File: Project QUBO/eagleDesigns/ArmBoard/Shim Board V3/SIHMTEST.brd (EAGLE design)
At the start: 71.1 x 81.3 mm, 30 parts, among them IC1 MCP2551/SN, U1 BME280

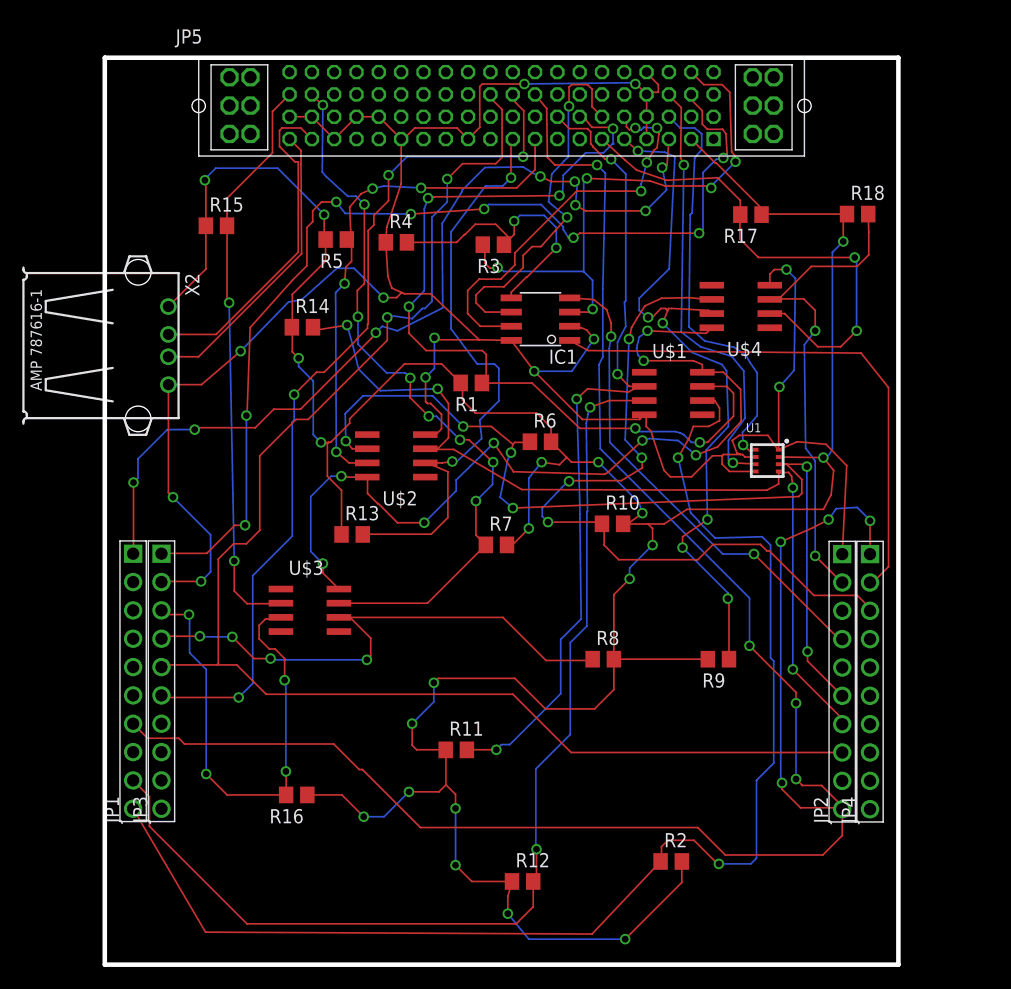
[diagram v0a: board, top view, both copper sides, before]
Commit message: 
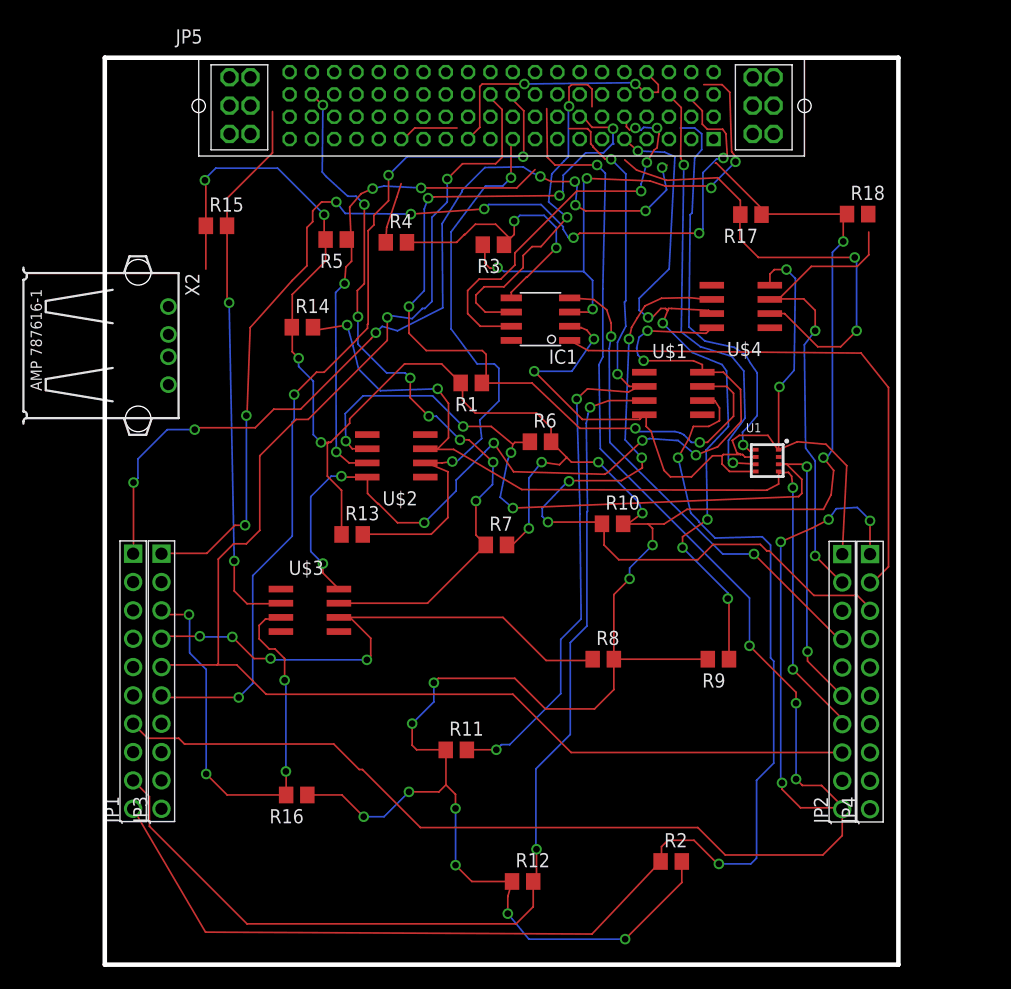
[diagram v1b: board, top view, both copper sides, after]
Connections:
- net N$11 renamed RX_CF
- net N$13 renamed CTS_CF
- net N$14 renamed RTS_CF
- net N$29 renamed CTS_MC
- net N$30 renamed RTS_MC
- net N$31 renamed PWM_0
- net N$48 renamed RX_SF
- net N$52 renamed CE_2
- net N$53 renamed CE_3
- net N$54 renamed CE_4
- net N$66 renamed RX_MD
- net N$67 renamed TX_MD
- net N$68 renamed CTS_MD
- net N$69 renamed RTS_MD
- net N$7 renamed RX_PF
- net N$73 renamed CE_LEDS
- net N$74 renamed CE_CPU
- net N$8 renamed TX_PF
- net UNBUFFERSCL0 renamed ACT_UNBUFFERSCL
- net UNBUFFERSCL1 renamed EXT_UNBUFFERSCL
- net UNBUFFERSCL2 renamed BATT_UNBUFFERSCL
- net UNBUFFERSCL3 renamed INT_UNBUFFERSCL
- net UNBUFFERSDA0 renamed ACT_UNBUFFERSDA
- net UNBUFFERSDA1 renamed EXT_UNBUFFERSDA
- net UNBUFFERSDA2 renamed BATT_UNBUFFERSDA
- net UNBUFFERSDA3 renamed INT_UNBUFFERSDA
- removed net 3.3(VDDBME): JP5.23, U1.P$8
- removed net 3.3(VDDIOBME): JP5.43, U1.P$6
- removed net 5.0(BME): JP5.2, R1.2, R10.2, R11.1, R12.1, R13.1, R14.1, R15.1, R16.1, R17.1, R18.1, R2.2, R5.2, R6.2, R7.2, R8.2, R9.2, U1.P$2, X2.1
- removed net BUFFERSCL0: JP5.28, R11.2, U$1.2
- removed net BUFFERSCL1: JP5.10, R13.2, U$2.2
- removed net BUFFERSCL2: JP5.60, R15.2, U$3.2
- removed net BUFFERSCL3: JP5.6, R17.2, U$4.2
- removed net BUFFERSDA0: JP5.27, R1.1, U$1.7
- removed net BUFFERSDA1: JP5.9, R5.1, U$2.7
- removed net BUFFERSDA2: JP5.59, R7.1, U$3.7
- removed net BUFFERSDA3: JP5.5, R9.1, U$4.7
- removed net BUFFERVCC(5V): JP5.22
- removed net GND: IC1.2, IC1.8, JP2.P$1, JP3.P$2, JP5.12, JP5.15, JP5.18, JP5.24, JP5.36, JP5.37, JP5.39, JP5.4, JP5.40, JP5.44, JP5.64, R4.1, U$1.4, U$2.4, U$4.4, U1.P$1, U1.P$5, U1.P$7, X2.4
- removed net GPIO_1: JP5.38
- removed net N$1: JP5.1
- removed net N$21: JP5.21
- removed net N$32: JP5.32
- removed net N$33: JP5.33
- removed net N$34: JP5.34
- removed net N$35: JP5.35
- removed net N$41: JP5.41
- removed net N$45: JP5.45
- removed net N$46: JP5.46
- removed net N$47: JP5.47
- removed net N$55: JP5.55
- removed net N$56: JP5.56
- removed net N$57: JP5.57
- removed net N$58: JP5.58
- removed net N$61: JP5.61
- removed net N$63: JP5.63
- removed net N$65: JP5.65
- removed net N$70: JP5.70
- removed net N$71: JP5.71
- removed net N$72: JP5.72
- removed net N$75: JP5.75
- removed net N$76: JP5.76
- removed net N$77: JP5.77
- removed net N$78: JP5.78
- removed net N$79: JP5.79
- removed net N$80: JP5.80
- removed net USB1+: JP5.17
- removed net USB1-: JP5.16
- removed net VDD: IC1.3, JP5.62, R3.2
- new net 12V: JP5.16, JP5.36, JP5.56, JP5.76
- new net 3.3V: JP5.18, JP5.38, JP5.58, JP5.78, U1.P$6, U1.P$8
- new net 5V: IC1.3, JP5.17, JP5.37, JP5.57, JP5.77, R1.2, R10.2, R11.1, R12.1, R13.1, R14.1, R15.1, R16.1, R17.1, R18.1, R2.2, R3.2, R5.2, R6.2, R7.2, R8.2, R9.2, U1.P$2, X2.1
- new net ACT_SCL: JP5.24, R11.2, U$1.2
- new net ACT_SDA: JP5.23, R1.1, U$1.7
- new net AGND: JP5.19, JP5.20, JP5.39, JP5.40, JP5.59, JP5.60, JP5.79, JP5.80
- new net BATT_SCL: JP5.44, R15.2, U$3.2
- new net BATT_SDA: JP5.43, R7.1, U$3.7
- new net CTS_MF: JP5.5
- new net CTS_PF: JP5.9
- new net CTS_SF: JP5.50
- new net DGND: IC1.2, IC1.8, JP2.P$1, JP3.P$2, JP5.1, JP5.15, JP5.21, JP5.25, JP5.32, JP5.35, JP5.47, JP5.55, JP5.63, JP5.75, R4.1, U$1.4, U$2.4, U$4.4, U1.P$1, U1.P$5, U1.P$7, X2.4
- new net EXT_SCL: JP5.34, R13.2, U$2.2
- new net EXT_SDA: JP5.33, R5.1, U$2.7
- new net GPIO: JP5.2, JP5.22
- new net GPIO_42: JP5.42
- new net GPIO_62: JP5.62
- new net INT_SCL: JP5.65, R17.2, U$4.2
- new net INT_SDA: JP5.64, R9.1, U$4.7
- new net PWM_1: JP5.26
- new net RTS_MF: JP5.6
- new net RTS_PF: JP5.10
- new net RTS_SF: JP5.51
- new net RX_MC: JP5.27
- new net RX_MF: JP5.3
- new net TX_CF: JP5.12
- new net TX_MC: JP5.28
- new net TX_MF: JP5.4
- new net TX_SF: JP5.49
- net 3.3(1): no longer JP5.3
- net 5.0(3): no longer JP5.42
- net CANH: now also JP5.45; no longer JP5.25
- net CANL: now also JP5.46; no longer JP5.26
- net MISO: now also JP5.72; no longer JP5.51
- net MOSI: now also JP5.71; no longer JP5.50
- net SPI_CLK: now also JP5.70; no longer JP5.49
- net USB_N: now also JP5.61; no longer JP5.19
- net USB_P: now also JP5.41; no longer JP5.20
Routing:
- net 5V: track 0.00 -> 321.1 mm, vias 0 -> 25
- net 5.0(BME): track 284.5 -> 0.00 mm, vias 20 -> 0
- net GND: track 222.6 -> 0.00 mm, vias 12 -> 0
- net DGND: track 0.00 -> 92.1 mm, vias 0 -> 4
- net BUFFERSDA0: track 78.1 -> 0.00 mm, vias 6 -> 0
- net ACT_SDA: track 0.00 -> 77.8 mm, vias 0 -> 6
- net 3.3V: track 0.00 -> 75.3 mm, vias 0 -> 3
- net BUFFERSCL0: track 74.2 -> 0.00 mm, vias 4 -> 0
- net ACT_SCL: track 0.00 -> 72.7 mm, vias 0 -> 4
- net BATT_SCL: track 0.00 -> 70.0 mm, vias 0 -> 4
- net INT_SDA: track 0.00 -> 68.5 mm, vias 0 -> 6
- net BUFFERSDA2: track 66.4 -> 0.00 mm, vias 8 -> 0
- net BATT_SDA: track 0.00 -> 66.3 mm, vias 0 -> 8
- net BUFFERSDA3: track 65.5 -> 0.00 mm, vias 6 -> 0
- net BUFFERSCL1: track 53.3 -> 0.00 mm, vias 2 -> 0
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- added copper zone on layer 16, net DGND
- removed copper zone on layer 16, net GND

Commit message: 
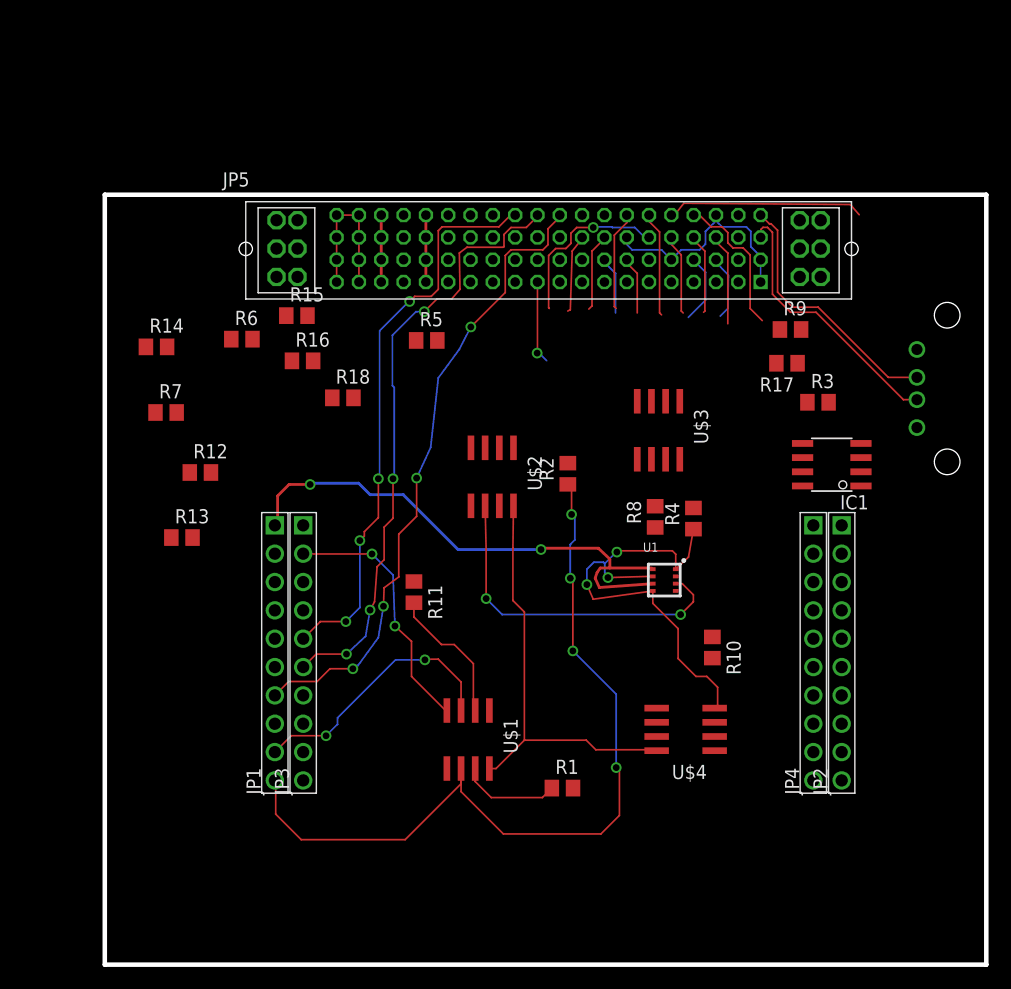
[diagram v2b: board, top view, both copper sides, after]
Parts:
- moved X2 93.1 mm to (85.8, 51.6), flipped to the bottom
- moved R18 49.0 mm to (21.3, 50.8)
- moved R12 46.7 mm to (8.57, 44.1)
- moved R16 38.9 mm to (17.7, 54.1), turned to 0 degrees
- moved U$4 38.2 mm to (52.1, 21.1)
- moved R1 37.2 mm to (41.0, 15.8), turned to 0 degrees
- moved R4 36.4 mm to (52.8, 40.0), turned to 90 degrees
- moved U$1 36.1 mm to (32.6, 20.2), turned to 180 degrees
- moved R2 36.0 mm to (41.5, 44.0), turned to 90 degrees
- moved U$3 35.2 mm to (49.6, 47.9), turned to 180 degrees
- moved R3 32.3 mm to (63.9, 50.4), turned to 0 degrees
- moved R7 31.9 mm to (5.49, 49.5)
- moved R9 30.2 mm to (61.5, 56.9), turned to 0 degrees
- moved IC1 29.2 mm to (65.2, 44.8)
- moved R6 28.3 mm to (12.3, 56.1)
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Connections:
- removed net 3.3(1): JP1.P$1
- removed net 5.0(3): JP3.P$1
- removed net PD6: JP4.P$8
- removed net PD7: JP4.P$9
- removed net U1RX(USB+)-: JP1.P$3
- removed net U1TX(USB-)-: JP1.P$4
- removed net U3RX-: JP4.P$6
- removed net U3TX-: JP4.P$7
- removed net U4RX-: JP4.P$4
- removed net U4TX-: JP4.P$5
- removed net U5RX-: JP1.P$5
- removed net U5TX-: JP1.P$6
- removed net U7RX-: JP2.P$3
- removed net U7TX-: JP3.P$7
- net 3.3V: now also JP1.P$1
- net 5V: now also JP3.P$1
- net CANRX: no longer JP2.P$4
- net CTS_MF: now also JP3.P$10
- net MOSI: no longer JP3.P$10
- net RTS_MF: now also JP2.P$4
- net RX_CF: now also JP2.P$3
- net RX_MC: now also JP4.P$4
- net RX_MD: now also JP4.P$8
- net RX_MF: now also JP1.P$3
- net RX_PF: now also JP1.P$5
- net RX_SF: now also JP4.P$6
- net TX_CF: now also JP3.P$7
- net TX_MC: now also JP4.P$5
- net TX_MD: now also JP4.P$9
- net TX_MF: now also JP1.P$4
- net TX_PF: now also JP1.P$6
- net TX_SF: now also JP4.P$7
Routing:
- net 5V: track 321.1 -> 0.00 mm, vias 25 -> 0
- net SPI_CLK: track 189.6 -> 57.0 mm, vias 8 -> 4
- net 5.0(3): track 91.6 -> 0.00 mm, vias 8 -> 0
- net EXT_UNBUFFERSCL: track 81.8 -> 0.00 mm, vias 4 -> 0
- net MISO: track 130.9 -> 51.3 mm, vias 2 -> 4
- net 3.3(1): track 77.6 -> 0.00 mm, vias 8 -> 0
- net ACT_UNBUFFERSCL: track 95.2 -> 23.9 mm
- net INT_UNBUFFERSDA: track 67.8 -> 0.00 mm, vias 4 -> 0
- net ACT_SDA: track 77.8 -> 14.8 mm, vias 6 -> 0
- net BATT_SCL: track 70.0 -> 7.17 mm, vias 4 -> 0
- net BATT_SDA: track 66.3 -> 8.20 mm, vias 8 -> 0
- net INT_SDA: track 68.5 -> 13.4 mm, vias 6 -> 0
- net EXT_UNBUFFERSDA: track 84.5 -> 30.6 mm, vias 6 -> 2
- net ACT_SCL: track 72.7 -> 18.9 mm, vias 4 -> 0
- net EXT_SCL: track 53.0 -> 0.00 mm, vias 2 -> 0
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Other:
- board size 71.1 x 81.3 mm -> 79 x 69 mm

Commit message: 
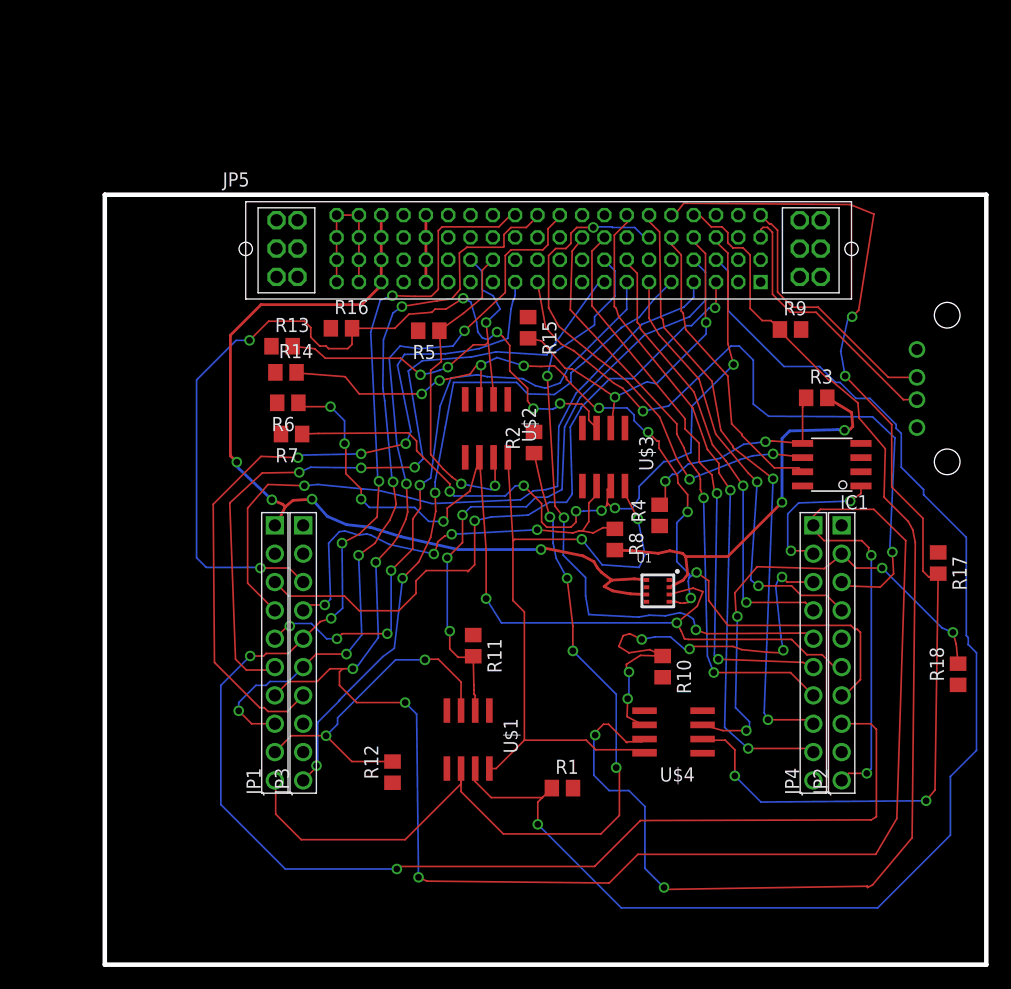
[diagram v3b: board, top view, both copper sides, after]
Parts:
- moved R18 60.4 mm to (76.5, 26.0), turned to 90 degrees
- moved R12 31.9 mm to (25.8, 17.3), turned to 90 degrees
- moved R17 22.5 mm to (74.7, 36.0), turned to 270 degrees
- moved R15 20.7 mm to (37.9, 57.1), turned to 270 degrees
- moved R13 19.4 mm to (15.9, 55.4)
- moved R14 11.8 mm to (16.2, 53.1)
- moved R7 11.4 mm to (16.7, 47.6), turned to 180 degrees
- moved R11 7.16 mm to (33.0, 28.6)
- moved R6 7.03 mm to (16.4, 50.4), turned to 180 degrees
- moved U$3 5.47 mm to (44.7, 45.5)
- moved R10 4.78 mm to (50.0, 26.7)
- moved R16 4.54 mm to (21.2, 57.0)
- moved U$2 4.37 mm to (34.2, 48.1)
- moved R8 4.14 mm to (45.7, 38.1), turned to 270 degrees
- moved R2 4.13 mm to (38.5, 46.8)
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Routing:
- net SPI_CLK: track 57.0 -> 195.9 mm, vias 4 -> 8
- net ACT_SDA: track 14.8 -> 119.4 mm, vias 0 -> 1
- net INT_SDA: track 13.4 -> 113.5 mm, vias 0 -> 2
- net MISO: track 51.3 -> 146.2 mm, vias 4 -> 6
- net DGND: track 84.8 -> 0.00 mm, vias 5 -> 0
- net EXT_UNBUFFERSCL: track 0.00 -> 84.1 mm, vias 0 -> 9
- net INT_SCL: track 17.8 -> 100.6 mm, vias 0 -> 4
- net BATT_UNBUFFERSCL: track 0.00 -> 77.7 mm, vias 0 -> 6
- net TX_CF: track 0.00 -> 66.8 mm, vias 0 -> 3
- net TX_PF: track 0.00 -> 66.1 mm, vias 0 -> 3
- net CTS_MF: track 0.00 -> 64.6 mm, vias 0 -> 3
- net TX_MF: track 0.00 -> 63.4 mm, vias 0 -> 1
- net RX_MF: track 0.00 -> 61.0 mm, vias 0 -> 2
- net BATT_SDA: track 8.20 -> 68.3 mm, vias 0 -> 6
- net RX_PF: track 0.00 -> 57.7 mm, vias 0 -> 5
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
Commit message: 
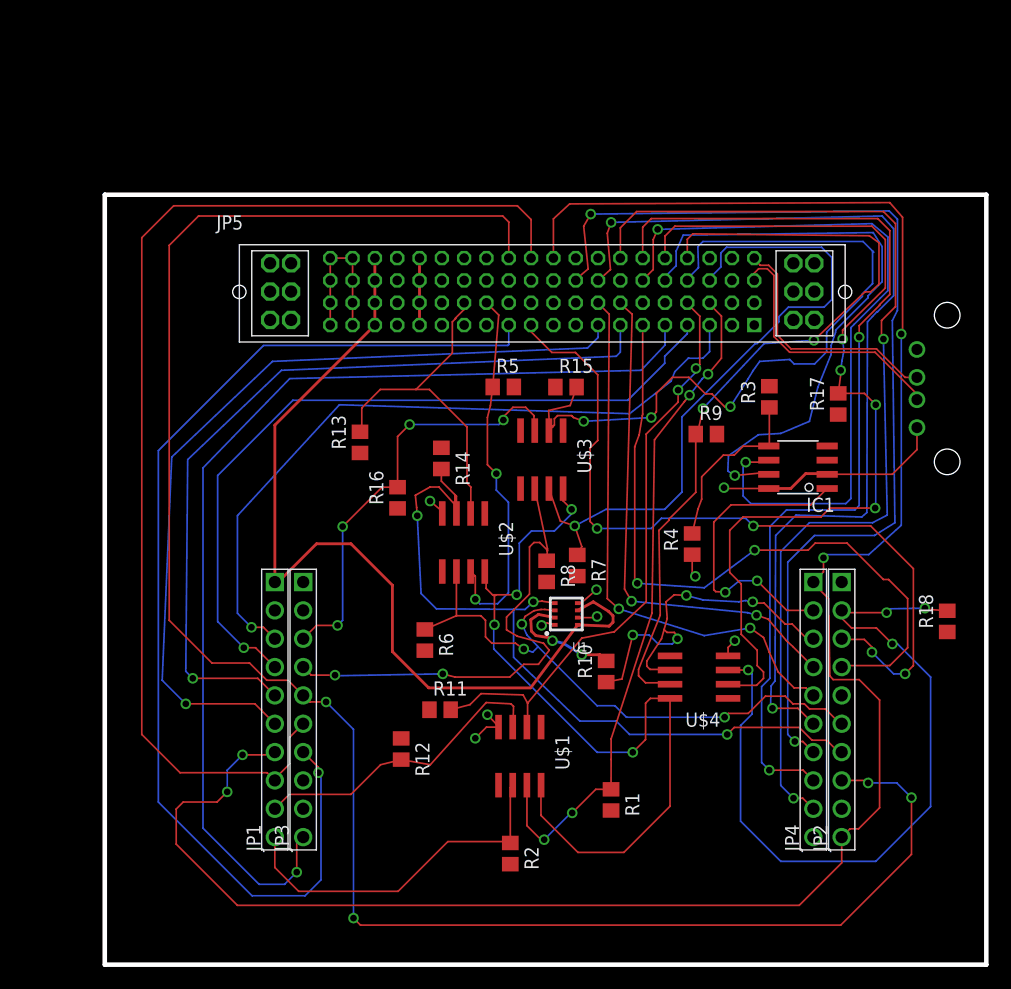
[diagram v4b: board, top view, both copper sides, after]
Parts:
- moved R2 36.9 mm to (36.3, 9.96), turned to 270 degrees
- moved R7 28.2 mm to (42.3, 35.8), turned to 270 degrees
- moved R6 24.6 mm to (28.7, 29.1), turned to 270 degrees
- moved R17 16.8 mm to (65.7, 50.2), turned to 90 degrees
- moved R16 16.0 mm to (26.2, 41.8), turned to 90 degrees
- moved R14 15.9 mm to (30.2, 45.4), turned to 270 degrees
- moved R9 12.0 mm to (53.9, 47.5)
- moved R13 11.1 mm to (22.9, 46.8), turned to 90 degrees
- moved U$2 10.4 mm to (32.2, 37.8)
- moved U1 8.47 mm to (41.4, 31.4), turned to 180 degrees
- moved R5 8.36 mm to (35.7, 51.8), turned to 0 degrees
- moved R8 6.75 mm to (39.6, 35.2)
- moved R11 6.46 mm to (30.0, 22.8), turned to 0 degrees
- moved R15 6.31 mm to (41.3, 51.8), turned to 0 degrees
- moved U$3 5.55 mm to (39.2, 45.3)
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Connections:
- removed net GPIO_42: JP5.42
- removed net GPIO_62: JP5.62
- net DGND: now also JP5.42, JP5.62
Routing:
- net ACT_SDA: track 119.4 -> 60.4 mm, vias 1 -> 4
- net ACT_UNBUFFERSDA: track 77.4 -> 31.9 mm, vias 4 -> 0
- net INT_SDA: track 113.5 -> 72.2 mm
- net BATT_UNBUFFERSCL: track 77.7 -> 38.7 mm, vias 6 -> 4
- net TX_SF: track 53.6 -> 91.1 mm
- net MOSI: track 67.5 -> 104.3 mm, vias 5 -> 0
- net BATT_SCL: track 32.0 -> 68.2 mm, vias 2 -> 3
- net RX_SF: track 51.1 -> 87.0 mm
- net DGND: track 0.00 -> 35.3 mm, vias 0 -> 9
- net RX_MD: track 53.8 -> 87.0 mm
- net TX_CF: track 66.8 -> 99.3 mm, vias 3 -> 1
- net TX_MD: track 58.5 -> 90.6 mm
- net CTS_MF: track 64.6 -> 94.2 mm, vias 3 -> 1
- net EXT_UNBUFFERSDA: track 82.5 -> 54.4 mm, vias 6 -> 3
- net CANH: track 26.8 -> 54.2 mm, vias 0 -> 1
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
